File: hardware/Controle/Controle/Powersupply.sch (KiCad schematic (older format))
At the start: 9 parts, among them U401 AP1117-3.3, U402 AP1117-5, U403 AP1117-15

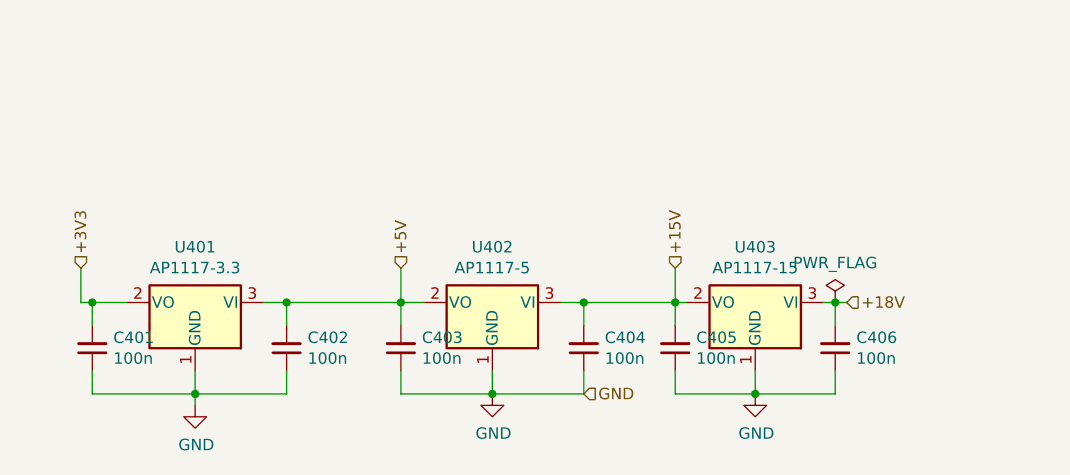
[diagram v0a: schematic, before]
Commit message: control PCB updated
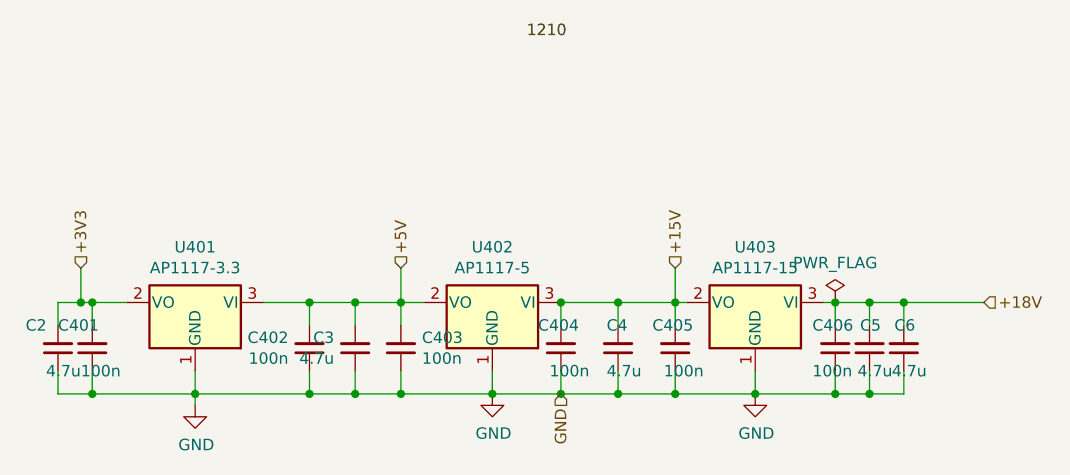
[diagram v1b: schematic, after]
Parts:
- added C2, C3, C4, C5, C6: 4.7u, Capacitor_SMD:C_1210_3225Metric_Pad1.33x2.70mm_HandSolder, symbol Device:C_Small
- U401, U402, U403: footprint Package_TO_SOT_SMD:SOT-223-3_TabPin2 -> KicadZeniteSolarLibrary18:TO-220-3_Horizontal_TabDown_SMD
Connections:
- net +15V: now also C4.2
- net +18V: now also C5.2, C6.2
- net +3V3: now also C2.2
- net +5V: now also C3.2
- net GND: now also C2.1, C3.1, C4.1, C5.1, C6.1
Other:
- moved on the sheet: C402, C404
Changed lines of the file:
@@
 Comment4 ""
 $EndDescr
-Wire Wire Line
-	6750 3700 6850 3700
 $Comp
 L power:GND #PWR?
@@
 AR Path="/60736CCE" Ref="C?"  Part="1"
 AR Path="/6072A37E/60736CCE" Ref="C401"  Part="1"
-F 0 "C401" H 4608 3854 50  0000 R CNN
-F 1 "100n" H 4608 3945 50  0000 R CNN
+F 0 "C401" H 4850 3800 50  0000 R CNN
+F 1 "100n" H 4750 4000 50  0000 R CNN
 F 2 "Capacitor_SMD:C_0603_1608Metric_Pad1.08x0.95mm_HandSolder" H 4700 3900 50  0001 C CNN
 F 3 "~" H 4700 3900 50  0001 C CNN
@@
 L Device:C_Small C?
 U 1 1 60736CDB
-P 5550 3900
+P 5650 3900
 AR Path="/60736CDB" Ref="C?"  Part="1"
 AR Path="/6072A37E/60736CDB" Ref="C402"  Part="1"
-F 0 "C402" H 5458 3854 50  0000 R CNN
-F 1 "100n" H 5458 3945 50  0000 R CNN
-F 2 "Capacitor_SMD:C_0603_1608Metric_Pad1.08x0.95mm_HandSolder" H 5550 3900 50  0001 C CNN
-F 3 "~" H 5550 3900 50  0001 C CNN
-	1    5550 3900
-	-1   0    0    1
-$EndComp
-Wire Wire Line
-	5550 3800 5550 3700
-Wire Wire Line
-	5450 3700 5550 3700
-Wire Wire Line
-	5550 4000 5550 4100
-Wire Wire Line
-	5550 4100 5150 4100
+F 0 "C402" H 5558 3854 50  0000 R CNN
+F 1 "100n" H 5558 3945 50  0000 R CNN
+F 2 "Capacitor_SMD:C_0603_1608Metric_Pad1.08x0.95mm_HandSolder" H 5650 3900 50  0001 C CNN
+F 3 "~" H 5650 3900 50  0001 C CNN
+	1    5650 3900
+	1    0    0    1
+$EndComp
+Wire Wire Line
+	5650 3800 5650 3700
+Wire Wire Line
+	5450 3700 5650 3700
+Wire Wire Line
+	5650 4000 5650 4100
 $Comp
 L Device:C_Small C?
 U 1 1 60736CE7
-P 6850 3900
+P 6750 3900
 AR Path="/60736CE7" Ref="C?"  Part="1"
 AR Path="/6072A37E/60736CE7" Ref="C404"  Part="1"
-F 0 "C404" H 6758 3854 50  0000 R CNN
-F 1 "100n" H 6758 3945 50  0000 R CNN
-F 2 "Capacitor_SMD:C_0603_1608Metric_Pad1.08x0.95mm_HandSolder" H 6850 3900 50  0001 C CNN
-F 3 "~" H 6850 3900 50  0001 C CNN
-	1    6850 3900
-	-1   0    0    1
-$EndComp
-Wire Wire Line
-	6850 3800 6850 3700
-Connection ~ 6850 3700
-Wire Wire Line
-	5550 3700 6050 3700
-Connection ~ 5550 3700
+F 0 "C404" H 6850 3800 50  0000 R CNN
+F 1 "100n" H 6800 4000 50  0000 R CNN
+F 2 "Capacitor_SMD:C_0603_1608Metric_Pad1.08x0.95mm_HandSolder" H 6750 3900 50  0001 C CNN
+F 3 "~" H 6750 3900 50  0001 C CNN
+	1    6750 3900
+	-1   0    0    1
+$EndComp
+Wire Wire Line
+	6750 3800 6750 3700
+Connection ~ 6750 3700
+Wire Wire Line
+	5650 3700 5850 3700
+Connection ~ 5650 3700
 $Comp
 L Device:C_Small C?
@@
 Wire Wire Line
 	6050 4000 6050 4100
-Wire Wire Line
-	6050 4100 6450 4100
 Connection ~ 6450 4100
 Wire Wire Line
 	6450 4000 6450 4100
 Wire Wire Line
-	6850 4100 6450 4100
-Wire Wire Line
-	6850 4000 6850 4100
-Text HLabel 8000 3700 2    50   Input ~ 0
+	6750 4100 6450 4100
+Wire Wire Line
+	6750 4000 6750 4100
+Text HLabel 8600 3700 2    50   Input ~ 0
 +18V
 Text HLabel 6050 3550 1    50   Input ~ 0
@@
 Text HLabel 4650 3550 1    50   Input ~ 0
 +3V3
-Text HLabel 6850 4100 2    50   Input ~ 0
+Text HLabel 6750 4100 3    50   Input ~ 0
 GND
 $Comp
@@
 F 0 "U403" H 7600 3942 50  0000 C CNN
 F 1 "AP1117-15" H 7600 3851 50  0000 C CNN
-F 2 "Package_TO_SOT_SMD:SOT-223-3_TabPin2" H 7600 3900 50  0001 C CNN
+F 2 "KicadZeniteSolarLibrary18:TO-220-3_Horizontal_TabDown_SMD" H 7600 3900 50  0001 C CNN
 F 3 "http://www.diodes.com/datasheets/AP1117.pdf" H 7700 3450 50  0001 C CNN
 	1    7600 3700
@@
 AR Path="/608B1292" Ref="C?"  Part="1"
 AR Path="/6072A37E/608B1292" Ref="C405"  Part="1"
-F 0 "C405" H 7158 3854 50  0000 R CNN
-F 1 "100n" H 7158 3945 50  0000 R CNN
+F 0 "C405" H 7350 3800 50  0000 R CNN
+F 1 "100n" H 7300 4000 50  0000 R CNN
 F 2 "Capacitor_SMD:C_0603_1608Metric_Pad1.08x0.95mm_HandSolder" H 7250 3900 50  0001 C CNN
 F 3 "~" H 7250 3900 50  0001 C CNN
@@
 	7250 3800 7250 3700
 Wire Wire Line
-	6850 3700 7250 3700
+	6750 3700 7000 3700
 Connection ~ 7250 3700
 Wire Wire Line
@@
 AR Path="/608B2E20" Ref="C?"  Part="1"
 AR Path="/6072A37E/608B2E20" Ref="C406"  Part="1"
-F 0 "C406" H 7858 3854 50  0000 R CNN
-F 1 "100n" H 7858 3945 50  0000 R CNN
+F 0 "C406" H 8050 3800 50  0000 R CNN
+F 1 "100n" H 8050 4000 50  0000 R CNN
 F 2 "Capacitor_SMD:C_0603_1608Metric_Pad1.08x0.95mm_HandSolder" H 7950 3900 50  0001 C CNN
 F 3 "~" H 7950 3900 50  0001 C CNN
@@
 Connection ~ 7950 3700
 Wire Wire Line
-	7950 3700 8000 3700
+	7950 3700 8100 3700
 Text HLabel 7250 3550 1    50   Input ~ 0
 +15V
@@
 F 0 "U402" H 6450 3942 50  0000 C CNN
 F 1 "AP1117-5" H 6450 3851 50  0000 C CNN
-F 2 "Package_TO_SOT_SMD:SOT-223-3_TabPin2" H 6450 3900 50  0001 C CNN
+F 2 "KicadZeniteSolarLibrary18:TO-220-3_Horizontal_TabDown_SMD" H 6450 3900 50  0001 C CNN
 F 3 "http://www.diodes.com/datasheets/AP1117.pdf" H 6550 3450 50  0001 C CNN
 	1    6450 3700
@@
 F 0 "U401" H 5150 3942 50  0000 C CNN
 F 1 "AP1117-3.3" H 5150 3851 50  0000 C CNN
-F 2 "Package_TO_SOT_SMD:SOT-223-3_TabPin2" H 5150 3900 50  0001 C CNN
+F 2 "KicadZeniteSolarLibrary18:TO-220-3_Horizontal_TabDown_SMD" H 5150 3900 50  0001 C CNN
 F 3 "http://www.diodes.com/datasheets/AP1117.pdf" H 5250 3450 50  0001 C CNN
 	1    5150 3700
 	-1   0    0    -1
 $EndComp
+$Comp
+L Device:C_Small C?
+U 1 1 6074CA2F
+P 5850 3900
+AR Path="/6074CA2F" Ref="C?"  Part="1"
+AR Path="/6072A37E/6074CA2F" Ref="C3"  Part="1"
+F 0 "C3" H 5758 3854 50  0000 R CNN
+F 1 "4.7u" H 5758 3945 50  0000 R CNN
+F 2 "Capacitor_SMD:C_1210_3225Metric_Pad1.33x2.70mm_HandSolder" H 5850 3900 50  0001 C CNN
+F 3 "~" H 5850 3900 50  0001 C CNN
+	1    5850 3900
+	1    0    0    1
+$EndComp
+Wire Wire Line
+	5850 4000 5850 4100
+Wire Wire Line
+	5150 4100 5650 4100
+Connection ~ 5650 4100
+Wire Wire Line
+	5650 4100 5850 4100
+Wire Wire Line
+	5850 4100 6050 4100
+Connection ~ 5850 4100
+Connection ~ 6050 4100
+Wire Wire Line
+	6050 4100 6450 4100
+Wire Wire Line
+	5850 3800 5850 3700
+Connection ~ 5850 3700
+Wire Wire Line
+	5850 3700 6050 3700
+$Comp
+L Device:C_Small C?
+U 1 1 6074EFA1
+P 4550 3900
+AR Path="/6074EFA1" Ref="C?"  Part="1"
+AR Path="/6072A37E/6074EFA1" Ref="C2"  Part="1"
+F 0 "C2" H 4500 3800 50  0000 R CNN
+F 1 "4.7u" H 4650 4000 50  0000 R CNN
+F 2 "Capacitor_SMD:C_1210_3225Metric_Pad1.33x2.70mm_HandSolder" H 4550 3900 50  0001 C CNN
+F 3 "~" H 4550 3900 50  0001 C CNN
+	1    4550 3900
+	1    0    0    1
+$EndComp
+$Comp
+L Device:C_Small C?
+U 1 1 6074FBAA
+P 8100 3900
+AR Path="/6074FBAA" Ref="C?"  Part="1"
+AR Path="/6072A37E/6074FBAA" Ref="C5"  Part="1"
+F 0 "C5" H 8150 3800 50  0000 R CNN
+F 1 "4.7u" H 8200 4000 50  0000 R CNN
+F 2 "Capacitor_SMD:C_1210_3225Metric_Pad1.33x2.70mm_HandSolder" H 8100 3900 50  0001 C CNN
+F 3 "~" H 8100 3900 50  0001 C CNN
+	1    8100 3900
+	1    0    0    1
+$EndComp
+Connection ~ 4650 3700
+Wire Wire Line
+	4550 3800 4550 3700
+Wire Wire Line
+	4550 3700 4650 3700
+Connection ~ 4700 4100
+Wire Wire Line
+	4550 4000 4550 4100
+Wire Wire Line
+	4550 4100 4700 4100
+$Comp
+L Device:C_Small C?
+U 1 1 6075CB1F
+P 7000 3900
+AR Path="/6075CB1F" Ref="C?"  Part="1"
+AR Path="/6072A37E/6075CB1F" Ref="C4"  Part="1"
+F 0 "C4" H 7050 3800 50  0000 R CNN
+F 1 "4.7u" H 7050 4000 50  0000 R CNN
+F 2 "Capacitor_SMD:C_1210_3225Metric_Pad1.33x2.70mm_HandSolder" H 7000 3900 50  0001 C CNN
+F 3 "~" H 7000 3900 50  0001 C CNN
+	1    7000 3900
+	-1   0    0    1
+$EndComp
+Wire Wire Line
+	7000 3800 7000 3700
+Connection ~ 7000 3700
+Wire Wire Line
+	7000 3700 7250 3700
+Wire Wire Line
+	7000 4100 6750 4100
+Wire Wire Line
+	7000 4000 7000 4100
+Connection ~ 6750 4100
+Wire Wire Line
+	7000 4100 7250 4100
+Connection ~ 7000 4100
+Connection ~ 7250 4100
+Wire Wire Line
+	8100 3800 8100 3700
+Connection ~ 8100 3700
+Wire Wire Line
+	8100 3700 8250 3700
+Wire Wire Line
+	8100 4100 8100 4000
+Connection ~ 7950 4100
+$Comp
+L Device:C_Small C?
+U 1 1 60775B6F
+P 8250 3900
+AR Path="/60775B6F" Ref="C?"  Part="1"
+AR Path="/6072A37E/60775B6F" Ref="C6"  Part="1"
+F 0 "C6" H 8300 3800 50  0000 R CNN
+F 1 "4.7u" H 8350 4000 50  0000 R CNN
+F 2 "Capacitor_SMD:C_1210_3225Metric_Pad1.33x2.70mm_HandSolder" H 8250 3900 50  0001 C CNN
+F 3 "~" H 8250 3900 50  0001 C CNN
+	1    8250 3900
+	1    0    0    1
+$EndComp
+Wire Wire Line
+	8250 3800 8250 3700
+Connection ~ 8250 3700
+Wire Wire Line
+	8250 4000 8250 4100
+Wire Wire Line
+	7950 4100 8100 4100
+Connection ~ 8100 4100
+Wire Wire Line
+	8100 4100 8250 4100
+Wire Wire Line
+	8250 3700 8600 3700
+Text Label 6600 2550 0    50   ~ 0
+1210
 $EndSCHEMATC

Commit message: Update Controle PCB
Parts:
- U401: value AP1117-3.3 -> AMS1117-3.3; footprint KicadZeniteSolarLibrary18:TO-220-3_Horizontal_TabDown_SMD -> Package_TO_SOT_SMD:SOT-223-3_TabPin2
- U402: value AP1117-5 -> AMS1117-5; footprint KicadZeniteSolarLibrary18:TO-220-3_Horizontal_TabDown_SMD -> Package_TO_SOT_SMD:SOT-223-3_TabPin2
- U403: value AP1117-15 -> K78L15-1000R3
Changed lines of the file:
@@
 P 7600 3700
 F 0 "U403" H 7600 3942 50  0000 C CNN
-F 1 "AP1117-15" H 7600 3851 50  0000 C CNN
+F 1 "K78L15-1000R3" H 7600 3851 50  0000 C CNN
 F 2 "KicadZeniteSolarLibrary18:TO-220-3_Horizontal_TabDown_SMD" H 7600 3900 50  0001 C CNN
-F 3 "http://www.diodes.com/datasheets/AP1117.pdf" H 7700 3450 50  0001 C CNN
+F 3 "" H 7700 3450 50  0001 C CNN
 	1    7600 3700
 	-1   0    0    -1
@@
 P 6450 3700
 F 0 "U402" H 6450 3942 50  0000 C CNN
-F 1 "AP1117-5" H 6450 3851 50  0000 C CNN
-F 2 "KicadZeniteSolarLibrary18:TO-220-3_Horizontal_TabDown_SMD" H 6450 3900 50  0001 C CNN
-F 3 "http://www.diodes.com/datasheets/AP1117.pdf" H 6550 3450 50  0001 C CNN
+F 1 "AMS1117-5" H 6450 3851 50  0000 C CNN
+F 2 "Package_TO_SOT_SMD:SOT-223-3_TabPin2" H 6450 3900 50  0001 C CNN
+F 3 "" H 6550 3450 50  0001 C CNN
 	1    6450 3700
 	-1   0    0    -1
@@
 P 5150 3700
 F 0 "U401" H 5150 3942 50  0000 C CNN
-F 1 "AP1117-3.3" H 5150 3851 50  0000 C CNN
-F 2 "KicadZeniteSolarLibrary18:TO-220-3_Horizontal_TabDown_SMD" H 5150 3900 50  0001 C CNN
-F 3 "http://www.diodes.com/datasheets/AP1117.pdf" H 5250 3450 50  0001 C CNN
+F 1 "AMS1117-3.3" H 5150 3851 50  0000 C CNN
+F 2 "Package_TO_SOT_SMD:SOT-223-3_TabPin2" H 5150 3900 50  0001 C CNN
+F 3 "" H 5250 3450 50  0001 C CNN
 	1    5150 3700
 	-1   0    0    -1

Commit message: first version of layout
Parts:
- removed U403: K78L15-1000R3, KicadZeniteSolarLibrary18:TO-220-3_Horizontal_TabDown_SMD, symbol Regulator_Linear:AP1117-15
- added U403: K78L15-1000R3, KicadZeniteSolarLibrary18:TO-220-3_Horizontal_Tabless_SMD, symbol Regulator_Linear:LM7805_TO220
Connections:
- net +15V: now also U403.3 (VO)
- net +18V: now also U403.1 (VI)
- net GND: now also U403.2 (GND)
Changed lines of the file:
@@
 GND
-$Comp
-L Regulator_Linear:AP1117-15 U403
-U 1 1 608AFF81
-P 7600 3700
-F 0 "U403" H 7600 3942 50  0000 C CNN
-F 1 "K78L15-1000R3" H 7600 3851 50  0000 C CNN
-F 2 "KicadZeniteSolarLibrary18:TO-220-3_Horizontal_TabDown_SMD" H 7600 3900 50  0001 C CNN
-F 3 "" H 7700 3450 50  0001 C CNN
-	1    7600 3700
-	-1   0    0    -1
-$EndComp
 $Comp
 L Device:C_Small C?
@@
 Text Label 6600 2550 0    50   ~ 0
 1210
+$Comp
+L Regulator_Linear:LM7805_TO220 U403
+U 1 1 609F70B2
+P 7600 3700
+F 0 "U403" H 7600 3942 50  0000 C CNN
+F 1 "K78L15-1000R3" H 7600 3851 50  0000 C CNN
+F 2 "KicadZeniteSolarLibrary18:TO-220-3_Horizontal_Tabless_SMD" H 7600 3925 50  0001 C CIN
+F 3 "https://www.onsemi.cn/PowerSolutions/document/MC7800-D.PDF" H 7600 3650 50  0001 C CNN
+	1    7600 3700
+	-1   0    0    -1
+$EndComp
 $EndSCHEMATC

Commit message: falta acabamento
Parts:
- C2, C3, C4, C5, C6: footprint Capacitor_SMD:C_1210_3225Metric_Pad1.33x2.70mm_HandSolder -> Capacitor_SMD:C_1206_3216Metric_Pad1.33x1.80mm_HandSolder
- U401: footprint Package_TO_SOT_SMD:SOT-223-3_TabPin2 -> Package_TO_SOT_SMD:SOT-89-3
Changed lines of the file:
@@
 F 0 "U401" H 5150 3942 50  0000 C CNN
 F 1 "AMS1117-3.3" H 5150 3851 50  0000 C CNN
-F 2 "Package_TO_SOT_SMD:SOT-223-3_TabPin2" H 5150 3900 50  0001 C CNN
+F 2 "Package_TO_SOT_SMD:SOT-89-3" H 5150 3900 50  0001 C CNN
 F 3 "" H 5250 3450 50  0001 C CNN
 	1    5150 3700
@@
 F 0 "C3" H 5758 3854 50  0000 R CNN
 F 1 "4.7u" H 5758 3945 50  0000 R CNN
-F 2 "Capacitor_SMD:C_1210_3225Metric_Pad1.33x2.70mm_HandSolder" H 5850 3900 50  0001 C CNN
+F 2 "Capacitor_SMD:C_1206_3216Metric_Pad1.33x1.80mm_HandSolder" H 5850 3900 50  0001 C CNN
 F 3 "~" H 5850 3900 50  0001 C CNN
 	1    5850 3900
@@
 F 0 "C2" H 4500 3800 50  0000 R CNN
 F 1 "4.7u" H 4650 4000 50  0000 R CNN
-F 2 "Capacitor_SMD:C_1210_3225Metric_Pad1.33x2.70mm_HandSolder" H 4550 3900 50  0001 C CNN
+F 2 "Capacitor_SMD:C_1206_3216Metric_Pad1.33x1.80mm_HandSolder" H 4550 3900 50  0001 C CNN
 F 3 "~" H 4550 3900 50  0001 C CNN
 	1    4550 3900
@@
 F 0 "C5" H 8150 3800 50  0000 R CNN
 F 1 "4.7u" H 8200 4000 50  0000 R CNN
-F 2 "Capacitor_SMD:C_1210_3225Metric_Pad1.33x2.70mm_HandSolder" H 8100 3900 50  0001 C CNN
+F 2 "Capacitor_SMD:C_1206_3216Metric_Pad1.33x1.80mm_HandSolder" H 8100 3900 50  0001 C CNN
 F 3 "~" H 8100 3900 50  0001 C CNN
 	1    8100 3900
@@
 F 0 "C4" H 7050 3800 50  0000 R CNN
 F 1 "4.7u" H 7050 4000 50  0000 R CNN
-F 2 "Capacitor_SMD:C_1210_3225Metric_Pad1.33x2.70mm_HandSolder" H 7000 3900 50  0001 C CNN
+F 2 "Capacitor_SMD:C_1206_3216Metric_Pad1.33x1.80mm_HandSolder" H 7000 3900 50  0001 C CNN
 F 3 "~" H 7000 3900 50  0001 C CNN
 	1    7000 3900
@@
 F 0 "C6" H 8300 3800 50  0000 R CNN
 F 1 "4.7u" H 8350 4000 50  0000 R CNN
-F 2 "Capacitor_SMD:C_1210_3225Metric_Pad1.33x2.70mm_HandSolder" H 8250 3900 50  0001 C CNN
+F 2 "Capacitor_SMD:C_1206_3216Metric_Pad1.33x1.80mm_HandSolder" H 8250 3900 50  0001 C CNN
 F 3 "~" H 8250 3900 50  0001 C CNN
 	1    8250 3900
